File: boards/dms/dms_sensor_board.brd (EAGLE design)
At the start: 44.5 x 44.5 mm, 24 parts, among them Q1 IRLML5203

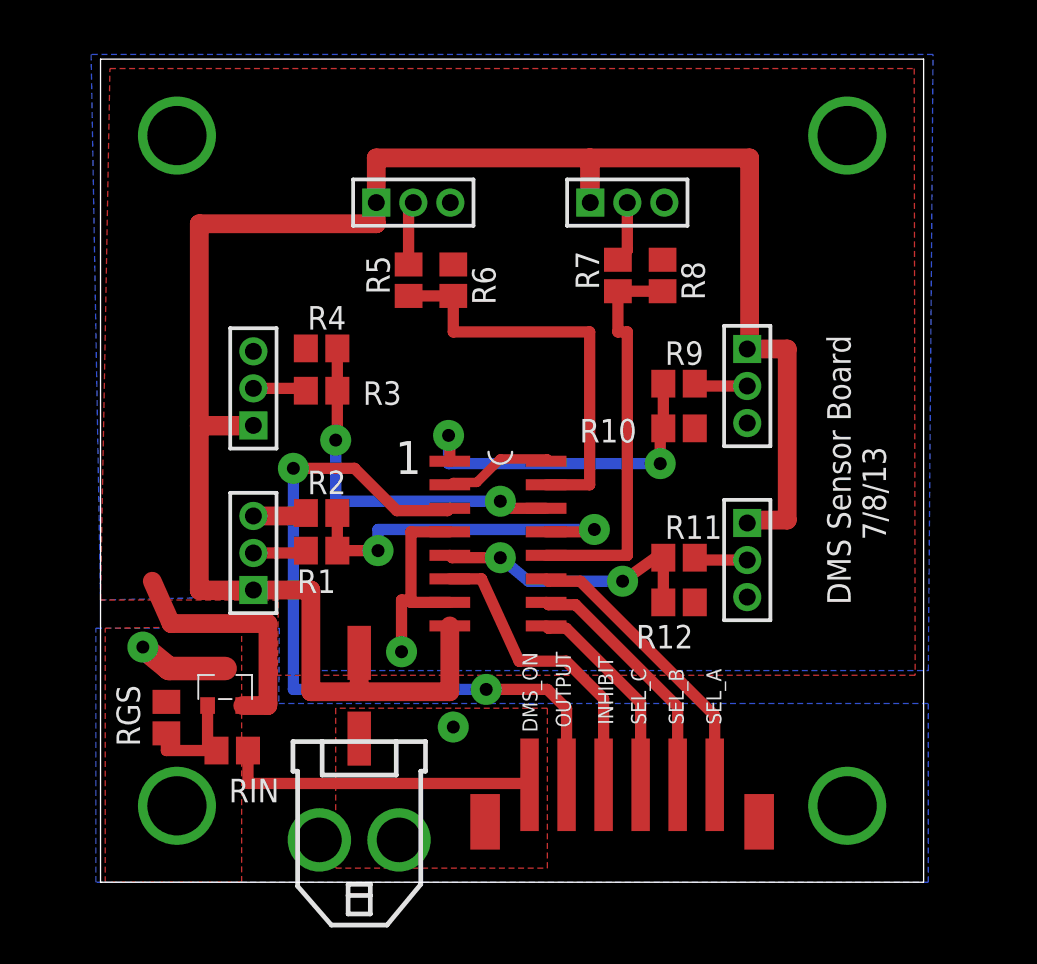
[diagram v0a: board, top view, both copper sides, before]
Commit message: Changing boards for fet and text improvements
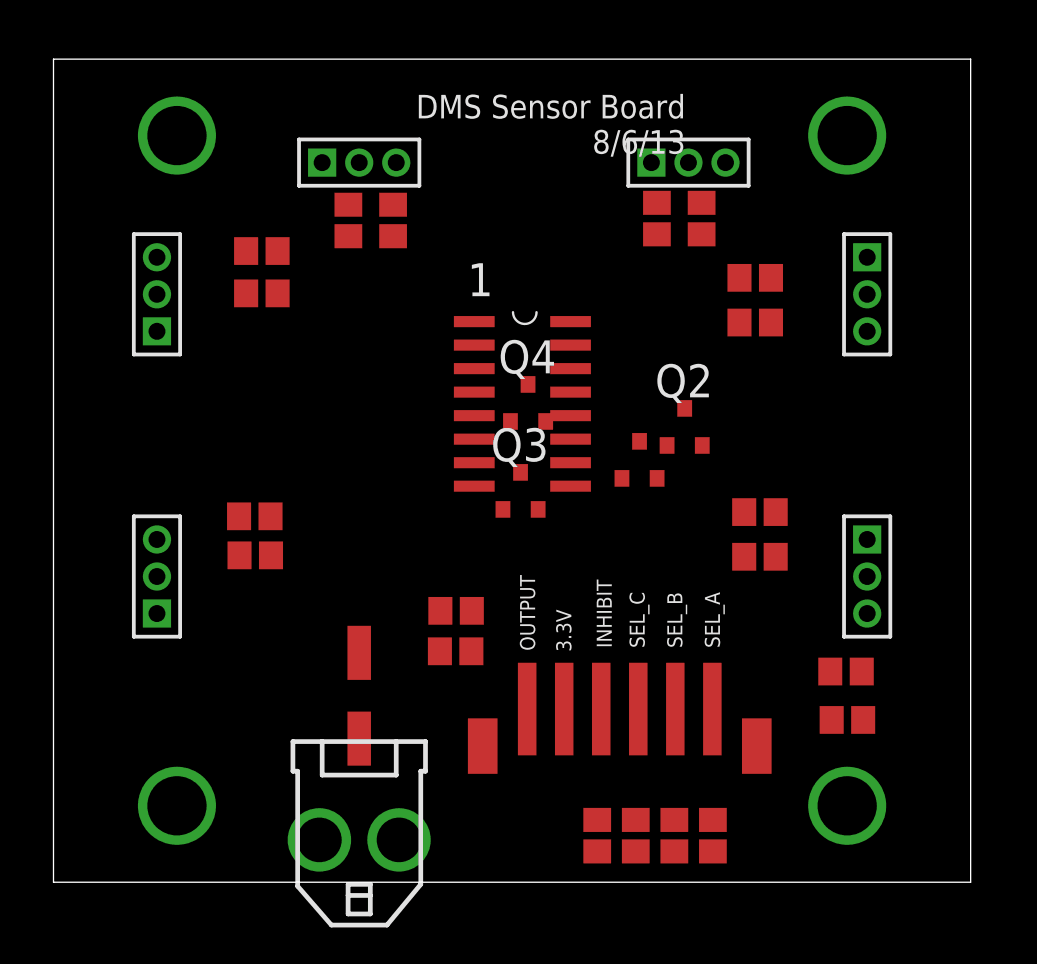
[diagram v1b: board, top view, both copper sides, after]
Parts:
- removed RGS, RIN: (no value), resistor:R0805
- added Q2, Q3, Q4: IRLML5203, ngohara_parts:MICRO3
- added R13, R14, R15, R16, R17, R18, R19, R20: 10K, resistor:R0805
- R1, R11, R3, R5, R7, R9: value (none) -> 200k
- R10, R12, R2, R4, R6, R8: value (none) -> 95.3k
- moved Q1 25.5 mm to (29.1, 22.8)
- moved JP5 8.15 mm to (41.4, 31.8)
- moved MUX1 7.66 mm to (22.8, 25.8)
- moved JP2 7.27 mm to (3.05, 31.8)
- moved R9 7.04 mm to (35.4, 32.6)
- moved R10 7.04 mm to (35.4, 30.2)
- moved JP6 6.54 mm to (41.4, 16.5)
- moved R3 6.17 mm to (8.71, 31.8)
- moved R4 6.17 mm to (8.71, 34.1)
- moved JP1 5.36 mm to (3.05, 16.5)
- moved R11 5.02 mm to (35.6, 20.0)
- moved R12 5.02 mm to (35.6, 17.6)
- moved R5 4.58 mm to (13.4, 35.7)
- moved R6 4.58 mm to (15.8, 35.7)
- moved U$2 4.09 mm to (20.1, 4.85)
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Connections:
- removed net DMS_ON: RIN.1, U$2.P$1
- removed net N$2: MUX1.10, U$2.P$5
- removed net N$3: MUX1.9, U$2.P$4
- removed net N$4: MUX1.6, U$2.P$3
- removed net N$8: Q1.1, RGS.1, RIN.2
- new net 3VCC: Q1.1, Q2.1, Q3.1, Q4.1, R14.1, R16.1, R18.1, R20.1, U$2.P$2
- new net A_H: Q1.2, R13.2
- new net B_H: Q2.2, R15.2
- new net C_H: Q3.2, R17.2
- new net IH_H: MUX1.6, Q4.2, R19.2
- new net INHIBIT: Q4.3, R20.2, U$2.P$3
- new net SEL_A: Q1.3, R14.2, U$2.P$6
- new net SEL_B: Q2.3, R16.2, U$2.P$5
- new net SEL_C: Q3.3, R18.2, U$2.P$4
- net 5V: now also R13.1, R15.1, R17.1, R19.1; no longer MUX1.8
- net GND: now also JP1.3, JP2.3, JP3.3, JP4.3, JP5.3, JP6.3, MUX1.7, MUX1.8, R10.1, R12.1, R2.1, R4.1, R6.1, R8.1; no longer Q1.3, RGS.2
- net N$1: now also MUX1.2; no longer MUX1.11, U$2.P$6
- net N$5: now also U$2.P$1; no longer U$2.P$2
- net N_GND: no longer JP1.3, JP2.3, JP3.3, JP4.3, JP5.3, JP6.3, MUX1.2, MUX1.7, Q1.2, R10.1, R12.1, R2.1, R4.1, R6.1, R8.1
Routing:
- net 5V: track 115.5 -> 0.00 mm
- net N$5: track 40.7 -> 0.00 mm, vias 2 -> 0
- net N_GND: track 33.5 -> 0.00 mm, vias 1 -> 0
- net DATA3-L: track 22.3 -> 0.00 mm
- net DATA4-L: track 21.6 -> 0.00 mm
- net DATA2-L: track 20.1 -> 0.00 mm, vias 2 -> 0
- net DATA1-L: track 19.8 -> 0.00 mm, vias 2 -> 0
- net DATA5-L: track 18.9 -> 0.00 mm, vias 2 -> 0
- net DMS_ON: track 17.1 -> 0.00 mm
- net N$4: track 16.7 -> 0.00 mm
- net N$1: track 15.9 -> 0.00 mm
- net DATA6-L: track 14.9 -> 0.00 mm, vias 2 -> 0
- net N$2: track 13.7 -> 0.00 mm
- net N$3: track 11.3 -> 0.00 mm
- net N$8: track 6.54 -> 0.00 mm
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- removed copper zone on layer 1, net GND
- removed copper zone on layer 16, net GND
- removed copper zone on layer 1, net N_GND
- removed copper zone on layer 16, net N_GND
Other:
- board size 44.5 x 44.5 mm -> 49.5 x 44.5 mm
- board text added: "3.3V"
- board text added: "DMS Sensor Board 8/6/13"
- board text removed: "DMS Sensor Board 7/8/13"
- board text removed: "DMS_ON"

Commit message: changes for new boards, cleared DRC
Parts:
- moved R19 24.2 mm to (18.8, 19.8), turned to 90 degrees
- moved R17 19.2 mm to (24.4, 22.2)
- moved R13 17.9 mm to (35.5, 22.1), turned to 180 degrees
- moved R15 15.0 mm to (30.7, 22.1), turned to 180 degrees
- moved Q1 7.34 mm to (35.6, 19.3), turned to 180 degrees
- moved Q4 6.75 mm to (21.6, 19.3), turned to 180 degrees
- moved Q2 5.35 mm to (30.7, 19.3), turned to 180 degrees
- moved R11 4.14 mm to (37.8, 16.5)
- moved Q3 3.93 mm to (26.2, 19.3), turned to 180 degrees
- moved R12 3.90 mm to (37.8, 14.4)
- moved MUX1 2.86 mm to (23.1, 28.7)
- moved R9 2.80 mm to (38.0, 31.7)
- moved R10 2.72 mm to (38.0, 29.7)
- moved R4 2.34 mm to (6.40, 33.7)
- moved R3 2.32 mm to (6.40, 31.6)
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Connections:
- removed net N$1: MUX1.2
- removed net N_GND: MUX1.16, MUX1.4
- net 5V: now also MUX1.16
- net A_H: now also MUX1.11
- net B_H: now also MUX1.10
- net C_H: now also MUX1.9
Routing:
- net 3VCC: track 0.00 -> 63.2 mm, vias 0 -> 5
- net DATA5-L: track 0.00 -> 59.7 mm
- net DATA6-L: track 0.00 -> 45.3 mm, vias 0 -> 2
- net 5V: track 0.00 -> 38.5 mm, vias 0 -> 4
- net N$5: track 0.00 -> 32.5 mm
- net DATA1-L: track 0.00 -> 31.4 mm, vias 0 -> 2
- net GND: track 0.00 -> 25.7 mm, vias 0 -> 2
- net DATA2-L: track 0.00 -> 22.2 mm, vias 0 -> 2
- net INHIBIT: track 0.00 -> 17.4 mm
- net SEL_C: track 0.00 -> 16.2 mm
- net SEL_A: track 0.00 -> 16.0 mm
- net A_H: track 0.00 -> 15.4 mm
- net SEL_B: track 0.00 -> 15.1 mm
- net DATA4-L: track 0.00 -> 14.6 mm
- net DATA3-L: track 0.00 -> 14.1 mm
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- added copper zone on layer 1, net 5V
- added copper zone on layer 16, net GND
